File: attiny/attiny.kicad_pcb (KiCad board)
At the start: 2 copper layers, 15.4 x 40.2 mm, 11 parts, among them J1 arduino, J2 esp32, J3 cavalier, J4 Conn_01x01, U1 ATtiny85V-10S

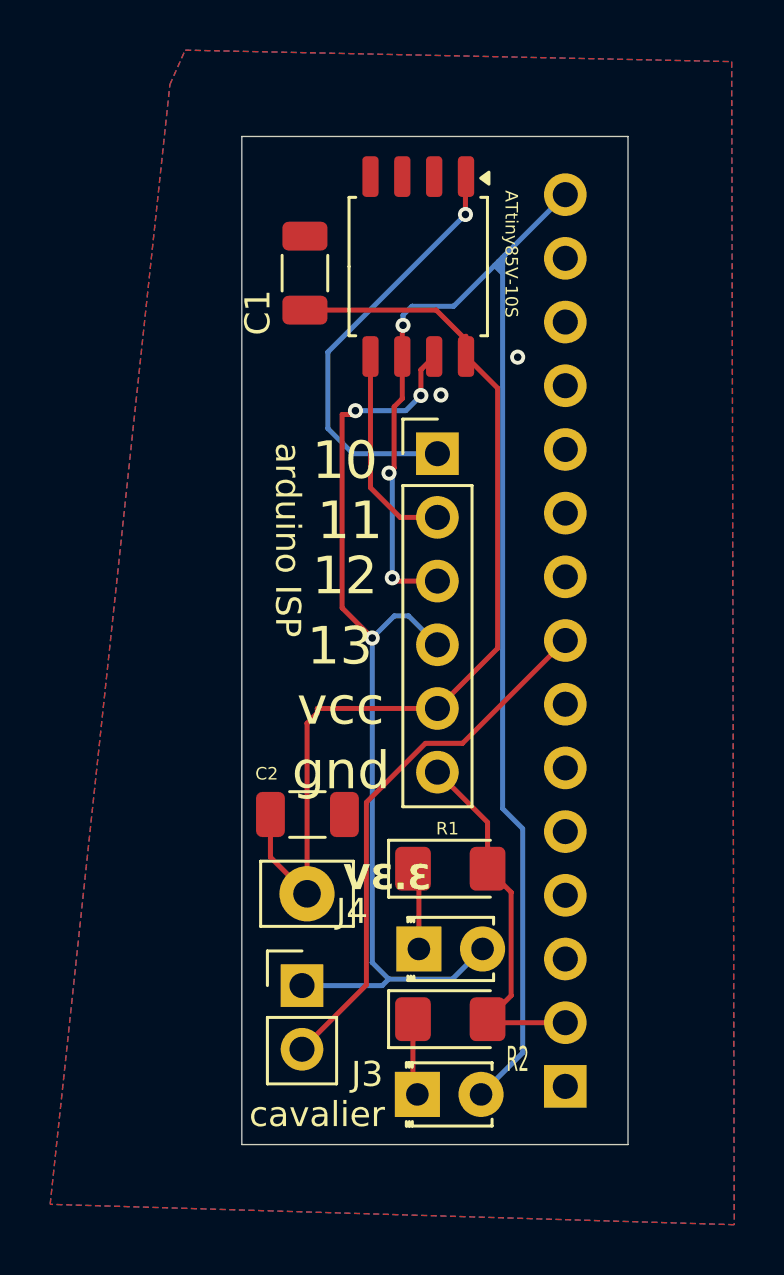
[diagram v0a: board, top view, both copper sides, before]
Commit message: correction erreur serigraphie + nouveau fichier de production
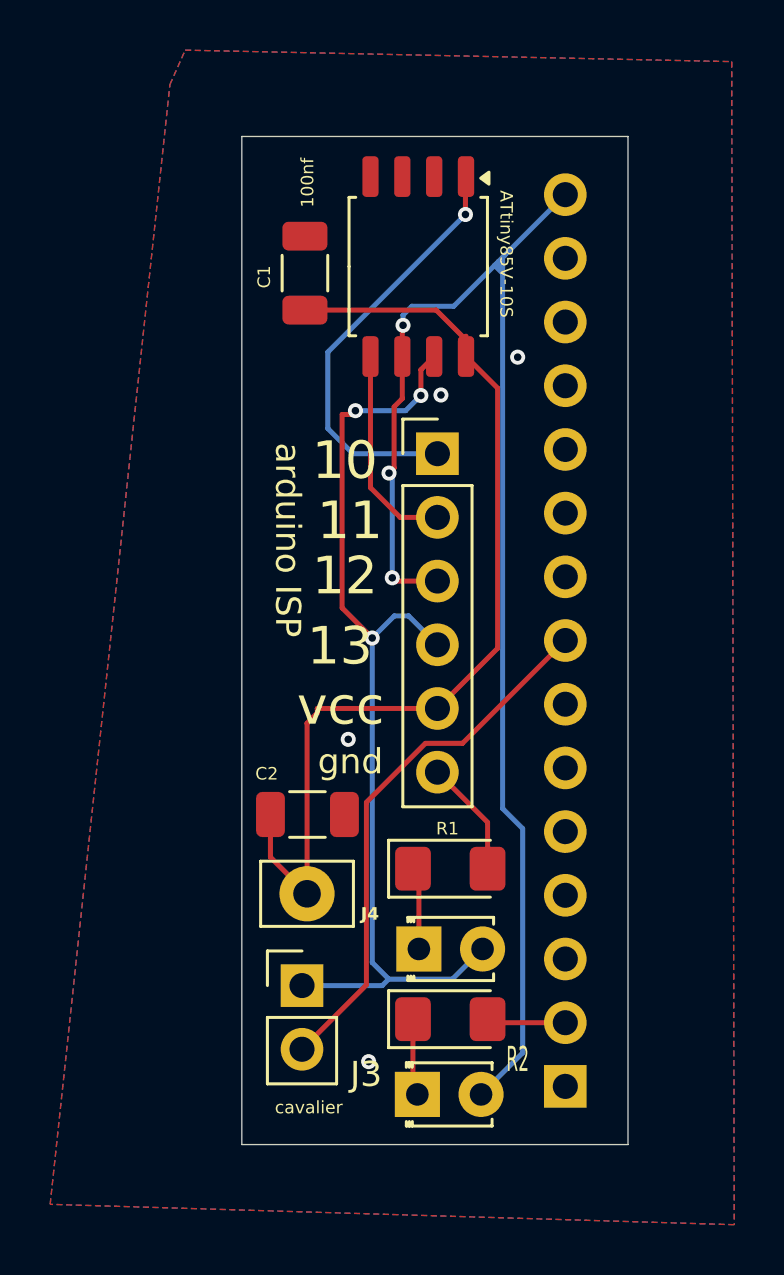
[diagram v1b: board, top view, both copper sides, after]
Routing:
- net GND: track 15.1 -> 8.29 mm, vias 2 -> 4
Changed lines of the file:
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@@
 		(tags "LED")
 		(property "Reference" "D2"
-			(at 0.7492 1.5888 0)
+			(at 1.308 1.6396 0)
 			(layer "B.SilkS")
 			(effects
 				(font
-					(size 1 1)
-					(thickness 0.15)
+					(size 0.5 0.5)
+					(thickness 0.1)
 				)
 				(justify mirror)
@@
 		(tags "Through hole pin header THT 1x02 2.54mm single row")
 		(property "Reference" "J3"
-			(at 2.6 3.54 0)
+			(at 2.5552 3.54 0)
 			(layer "F.SilkS")
 			(effects
@@
 		)
 		(property "Value" "cavalier"
-			(at 0.6 5.14 0)
-			(layer "F.SilkS")
-			(effects
-				(font
-					(size 1 1)
-					(thickness 0.15)
+			(at 0.2692 4.862 0)
+			(layer "F.SilkS")
+			(effects
+				(font
+					(size 0.5 0.5)
+					(thickness 0.05)
 				)
 			)
@@
 		(tags "capacitor")
 		(property "Reference" "C1"
-			(at -1.573 -1.8796 90)
-			(layer "F.SilkS")
-			(effects
-				(font
-					(size 1 1)
-					(thickness 0.15)
+			(at -0.1506 -1.6256 90)
+			(layer "F.SilkS")
+			(effects
+				(font
+					(size 0.5 0.5)
+					(thickness 0.05)
 				)
 			)
 		)
 		(property "Value" "100nf"
-			(at 2.7922 -1.7272 90)
-			(layer "F.Fab")
-			(effects
-				(font
-					(size 1 1)
-					(thickness 0.15)
+			(at 3.6086 0.1016 90)
+			(layer "F.SilkS")
+			(effects
+				(font
+					(size 0.5 0.5)
+					(thickness 0.125)
 				)
 			)
@@
 		(tags "solder Pin_ with flat fork")
 		(property "Reference" "J4"
-			(at 1.7964 0.6988 0)
-			(layer "F.SilkS")
-			(effects
-				(font
-					(size 1 1)
-					(thickness 0.15)
+			(at 2.5076 0.8004 0)
+			(layer "F.SilkS")
+			(effects
+				(font
+					(size 0.5 0.5)
+					(thickness 0.1)
+					(bold yes)
 				)
 			)
@@
 		)
 		(property "Value" "ATtiny85V-10S"
-			(at -0.5015 -3.7114 270)
+			(at -0.5015 -3.5082 270)
 			(unlocked yes)
 			(layer "F.SilkS")
@@
 				(font
 					(size 0.5 0.5)
-					(thickness 0.125)
+					(thickness 0.04)
 				)
 			)
@@
 	)
 	(gr_text "gnd"
-		(at 146.6 74.5744 0)
+		(at 147.6248 73.914 0)
 		(layer "F.SilkS")
 		(effects
 			(font
-				(size 1.5 1.5)
-				(thickness 0.1875)
+				(size 1 1)
+				(thickness 0.1)
 			)
 			(justify left bottom)
@@
 		)
 	)
-	(gr_text "3.3V"
-		(at 152.146 78.5368 0)
-		(layer "F.SilkS")
-		(effects
-			(font
-				(size 1 1)
-				(thickness 0.25)
-				(bold yes)
-			)
-			(justify left bottom mirror)
-		)
-	)
 	(gr_text "12"
 		(at 147.4 66.8 0)
@@
 		)
 	)
+	(gr_text "3.3V"
+		(at 152.146 78.5368 0)
+		(layer "B.SilkS")
+		(effects
+			(font
+				(size 1 1)
+				(thickness 0.25)
+				(bold yes)
+			)
+			(justify left bottom mirror)
+		)
+	)
 	(segment
 		(start 154.801 58.436)
@@
 	)
 	(segment
-		(start 155.341 82.659)
-		(end 155.341 78.541)
-		(width 0.2)
-		(layer "F.Cu")
-		(net 4)
-	)
-	(segment
 		(start 154.4 75.75)
 		(end 152.4 73.75)
@@
 		(net 4)
 	)
-	(segment
-		(start 154.4 83.6)
-		(end 155.341 82.659)
-		(width 0.2)
-		(layer "F.Cu")
-		(net 4)
-	)
-	(segment
-		(start 155.341 78.541)
-		(end 154.4 77.6)
-		(width 0.2)
-		(layer "F.Cu")
+	(via
+		(at 149.6568 85.2932)
+		(size 0.6)
+		(drill 0.3)
+		(layers "F.Cu" "B.Cu")
+		(free yes)
 		(net 4)
 	)
@@
 		(size 0.6)
 		(drill 0.3)
+		(layers "F.Cu" "B.Cu")
+		(free yes)
+		(net 4)
+	)
+	(via
+		(at 148.844 72.4408)
+		(size 0.6)
+		(drill 0.3)

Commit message: correction routage mineur
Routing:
- net GND: track 8.29 -> 9.88 mm
- net VCC: track 39.8 -> 38.6 mm
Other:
- board text added: "WDI"
- board text added: "reset"
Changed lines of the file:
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@@
 		(tags "LED")
 		(property "Reference" "D2"
-			(at 1.308 1.6396 0)
+			(at 1.3125 -3 0)
 			(layer "B.SilkS")
 			(effects
@@
 		)
 		(property "Value" "ATtiny85V-10S"
-			(at -0.5015 -3.5082 270)
+			(at -0.0443 -3.6098 270)
 			(unlocked yes)
 			(layer "F.SilkS")
@@
 	(gr_text "gnd"
 		(at 147.6248 73.914 0)
-		(layer "F.SilkS")
+		(layer "F.SilkS" knockout)
 		(effects
 			(font
@@
 		)
 	)
+	(gr_text "WDI"
+		(at 156.1084 69.1388 0)
+		(layer "B.SilkS" knockout)
+		(effects
+			(font
+				(size 0.8 0.8)
+				(thickness 0.125)
+			)
+			(justify left bottom mirror)
+		)
+	)
 	(gr_text "3.3V"
-		(at 152.146 78.5368 0)
+		(at 148.7932 76.8096 0)
 		(layer "B.SilkS")
 		(effects
@@
 		)
 	)
+	(gr_text "reset"
+		(at 155.8544 51.0032 0)
+		(layer "B.SilkS" knockout)
+		(effects
+			(font
+				(size 1 1)
+				(thickness 0.1)
+			)
+			(justify left bottom mirror)
+		)
+	)
+	(segment
+		(start 149.098 72.4916)
+		(end 147.2 74.3896)
+		(width 0.2)
+		(layer "F.Cu")
+		(net 1)
+	)
+	(segment
+		(start 152.4 71.21)
+		(end 151.1184 72.4916)
+		(width 0.2)
+		(layer "F.Cu")
+		(net 1)
+	)
 	(segment
 		(start 154.801 58.436)
@@
 	)
 	(segment
-		(start 147.2 71.8)
-		(end 147.2 78.2)
-		(width 0.2)
-		(layer "F.Cu")
-		(net 1)
-	)
-	(segment
-		(start 147.61 71.21)
-		(end 147.61 71.39)
+		(start 147.2 74.3896)
+		(end 147.2 78.6)
 		(width 0.2)
 		(layer "F.Cu")
@@
 	)
 	(segment
-		(start 147.61 71.39)
-		(end 147.2 71.8)
-		(width 0.2)
-		(layer "F.Cu")
-		(net 1)
-	)
-	(segment
 		(start 153.416 57.051)
 		(end 153.54 57.175)
@@
 	)
 	(segment
-		(start 152.4 71.21)
-		(end 147.61 71.21)
+		(start 151.1184 72.4916)
+		(end 149.098 72.4916)
 		(width 0.2)
 		(layer "F.Cu")
@@
 	)
 	(segment
+		(start 148.7424 75.3872)
+		(end 148.6916 75.438)
+		(width 0.2)
+		(layer "F.Cu")
+		(net 4)
+	)
+	(segment
 		(start 154.4 77.6)
 		(end 154.4 75.75)
@@
 		(start 157.5 83.74)
 		(end 154.54 83.74)
+		(width 0.2)
+		(layer "F.Cu")
+		(net 4)
+	)
+	(segment
+		(start 148.7424 73.8632)
+		(end 148.7424 75.3872)
 		(width 0.2)
 		(layer "F.Cu")
@@
 	)
 	(via
-		(at 148.844 72.4408)
+		(at 148.7424 73.8632)
 		(size 0.6)
 		(drill 0.3)

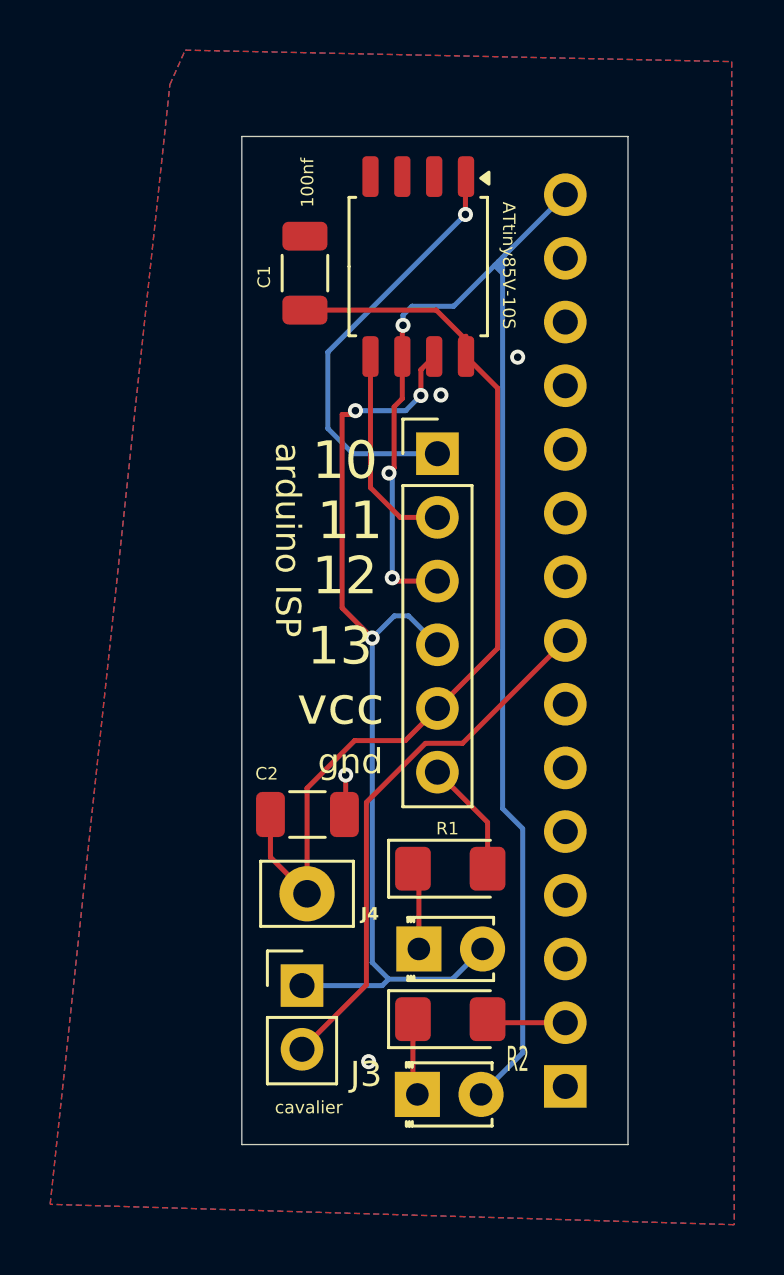
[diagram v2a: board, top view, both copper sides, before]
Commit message: composant basic pour jlpcb (très petit dificilement soudable a la main)
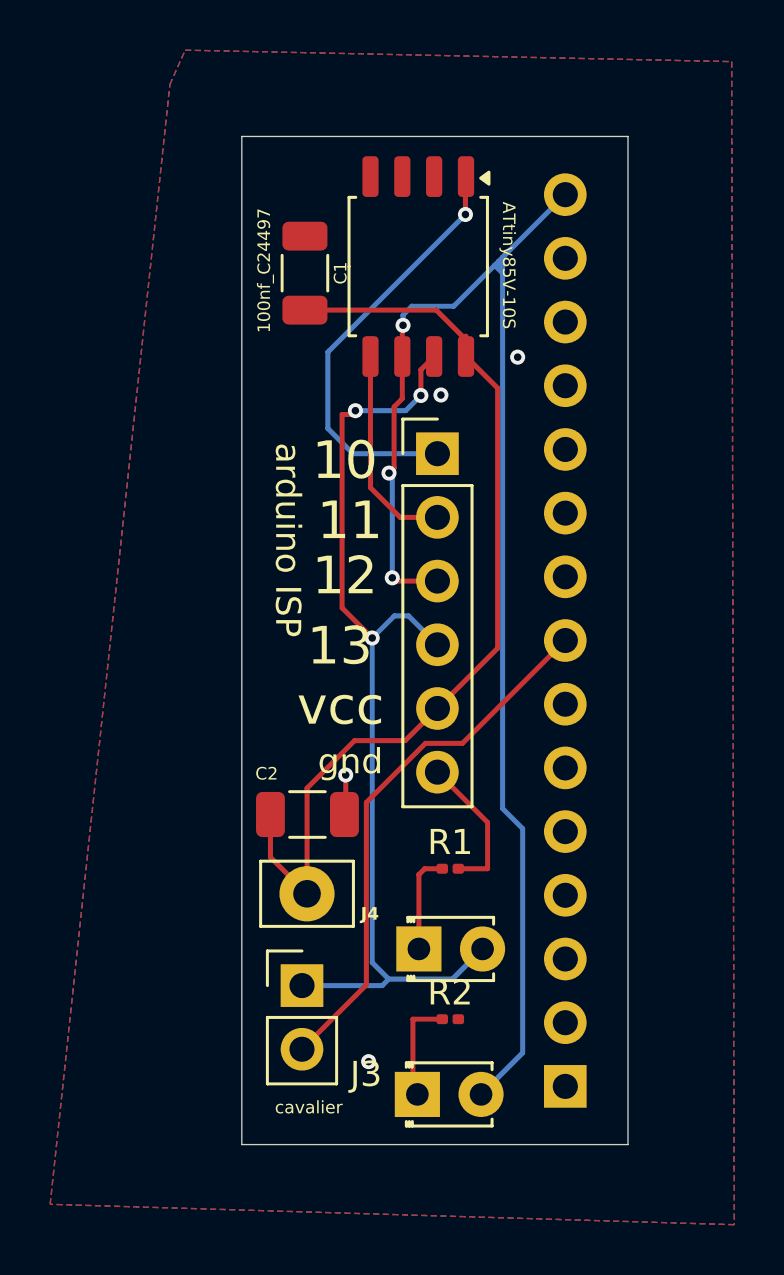
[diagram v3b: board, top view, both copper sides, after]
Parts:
- C1, C2: value 100nf -> 100nf_C24497
- R1: value R -> 12kΩ_C22790; footprint LED_SMD:LED_1206_3216Metric_Pad1.42x1.75mm_HandSolder -> Resistor_SMD:R_0201_0603Metric
- R2: value R -> 12kΩ _C22790; footprint LED_SMD:LED_1206_3216Metric_Pad1.42x1.75mm_HandSolder -> Resistor_SMD:R_0201_0603Metric
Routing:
- net GND: track 9.88 -> 7.89 mm
- net Net-(D2-K): track 3.07 -> 4.24 mm
- net Net-(D1-K): track 3.30 -> 3.99 mm
